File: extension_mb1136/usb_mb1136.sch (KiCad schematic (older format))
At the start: 1 part

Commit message: update schema
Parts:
- added C1: 4.7uF, symbol Device:CP
- added CNUSB_2: USB_A, symbol Connector:USB_A
- added D1: ESDALC6V1-1U2, Diode_SMD:D_0201_0603Metric, symbol Device:D
- added LD1: RED, Diode_SMD:D_0805_2012Metric, symbol Device:LED
- added LD2: GREEN, Diode_SMD:D_0805_2012Metric, symbol Device:LED
- added Q1: S9013, Package_TO_SOT_SMD:SOT-23, symbol Device:Q_NPN_BEC
- added R1: 620, Resistor_SMD:R_0805_2012Metric, symbol Device:R
- added R2, R6: 47K, Resistor_SMD:R_0805_2012Metric, symbol Device:R
- added R3: 430K, Resistor_SMD:R_0805_2012Metric, symbol Device:R
- added R4: 620K, Resistor_SMD:R_0805_2012Metric, symbol Device:R
- added R5: 330, Resistor_SMD:R_0805_2012Metric, symbol Device:R
- added R7: 22K, Resistor_SMD:R_0805_2012Metric, symbol Device:R
- added R7: 10K, Resistor_SMD:R_0805_2012Metric, symbol Device:R
- added U1: STMPS2151MTR, Package_SO:SO-8_3.9x4.9mm_P1.27mm, symbol st:STMPS2151MTR
- renumbered CNUSB to CNUSB_1
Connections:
- net USB_VBUS: now reaches CNUSB_1.1 (VBUS)
- net USB_VBUS: now also C1.1, CNUSB_2.1 (VBUS), R3.1, R6.1, U1.6 (OUT), U1.7 (OUT), U1.8 (OUT)
- net USB_DM: now reaches CNUSB_1.2 (D-)
- net USB_DM: now also CNUSB_2.2 (D-)
- net USB_DP: now reaches CNUSB_1.3 (D+)
- net USB_DP: now also CNUSB_2.3 (D+)
- net USB_ID: now reaches CNUSB_1.4 (ID)
- net USB_ID: now also D1.1 (K)
- net GND: now reaches CNUSB_1.5 (GND)
- net GND: now also CNUSB_1.6 (Shield), C1.2, CNUSB_2.4 (GND), CNUSB_2.5 (Shield), D1.2 (A), Q1.2 (E), R4.2, R7.2, R7.2, U1.1 (GND)
- new net: LD1.2 (A), R1.2
- new net: Q1.1 (B), R6.2, R7.1
- new net: LD2.1 (K), Q1.3 (C)
- new net: LD2.2 (A), R5.2
- new net +3V3: R1.1, R2.1, R5.1
- new net +5V: U1.2 (IN), U1.3 (IN)
- new net USB_OWER_CURRENT: LD1.1 (K), R2.2, U1.5 (~FAULT)
- new net USB_POWER_SWITCH_ON: R7.1, U1.4 (EN)
- new net VBUS_DET: R3.2, R4.1

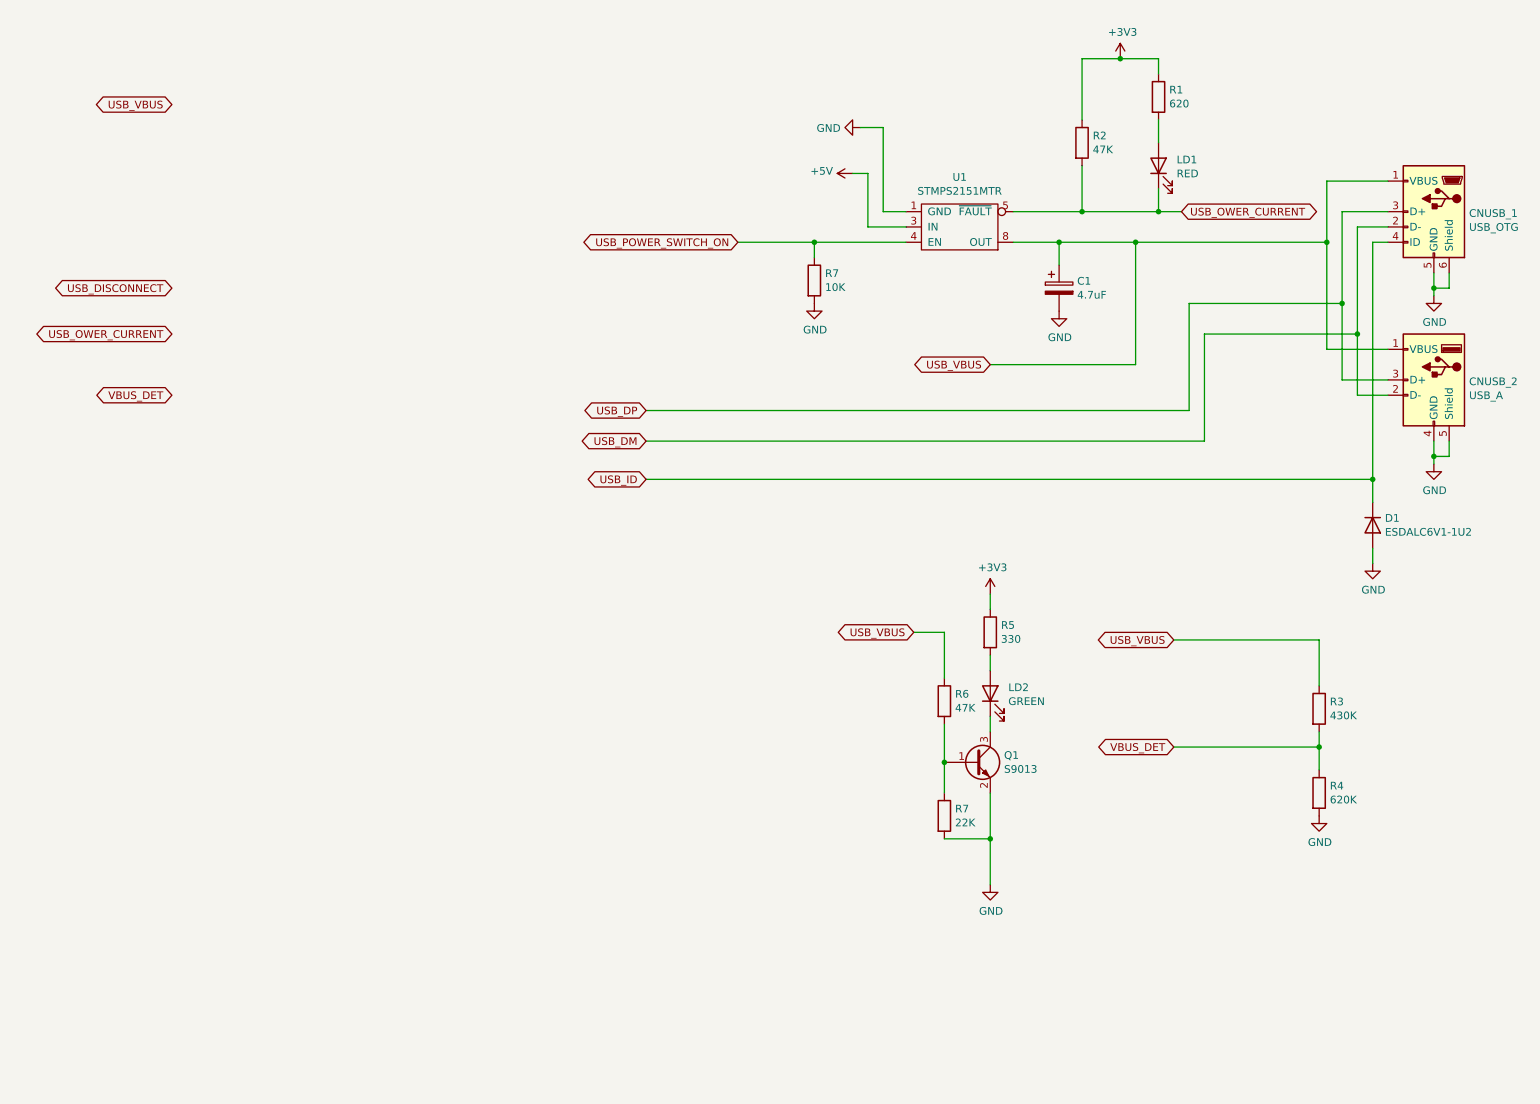
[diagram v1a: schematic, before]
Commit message: USB_connector
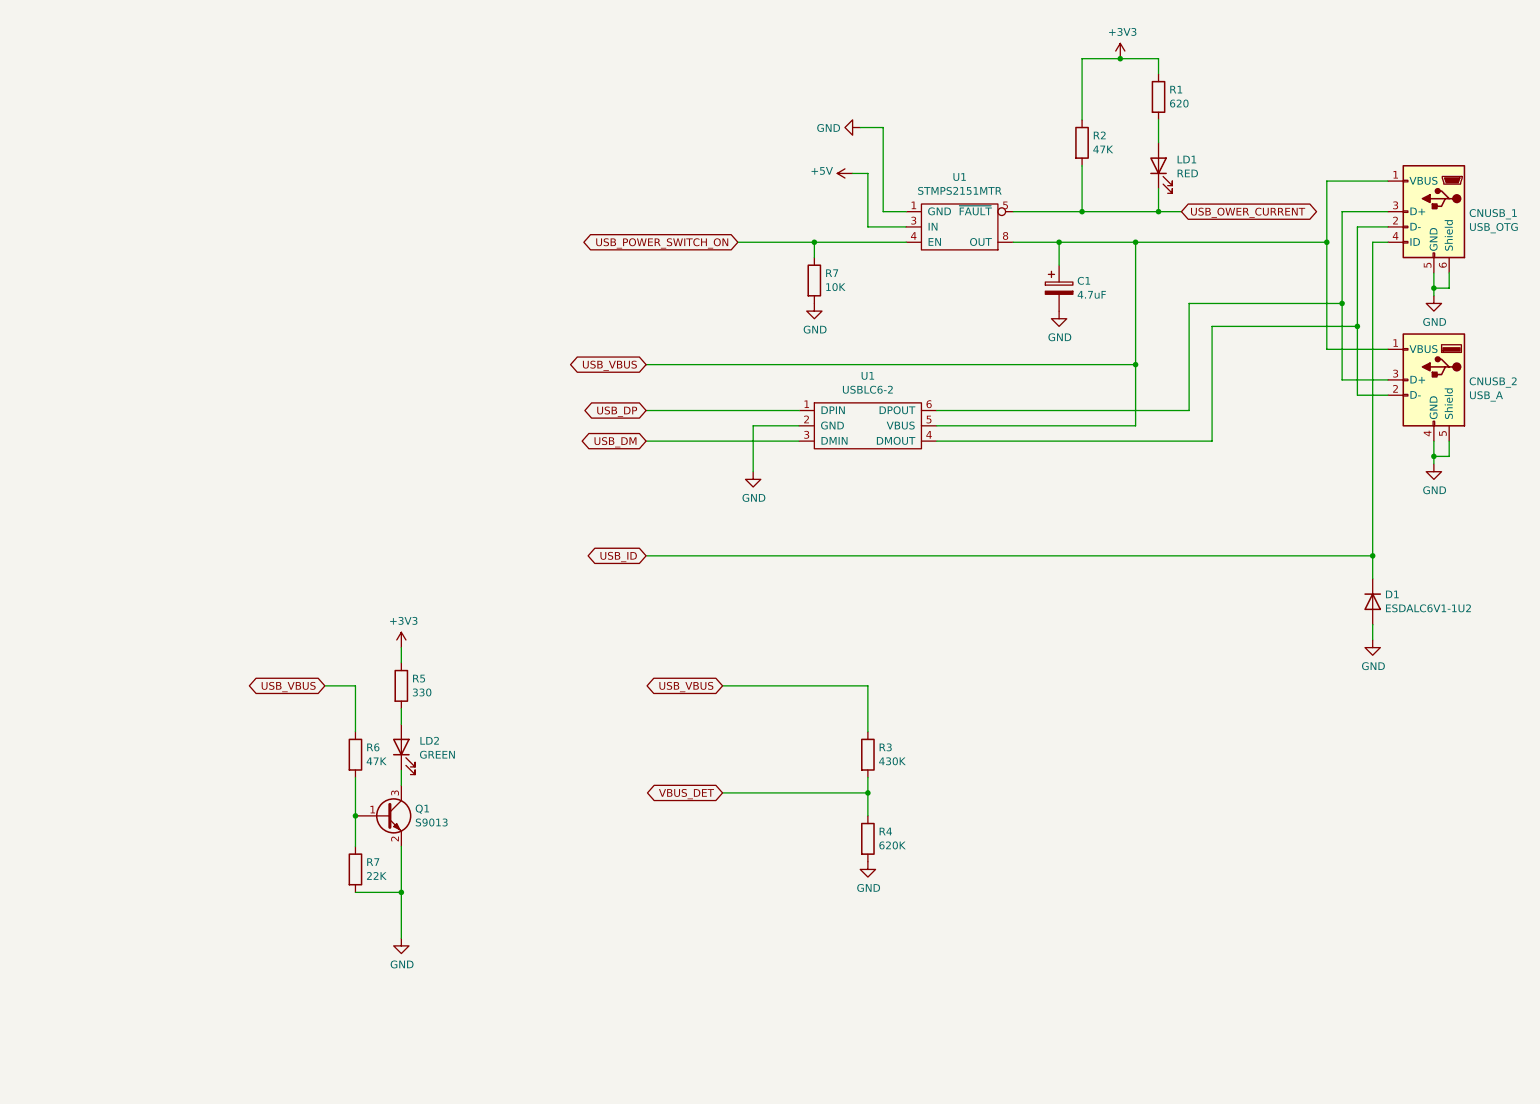
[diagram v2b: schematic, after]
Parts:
- added U1: USBLC6-2, Package_TO_SOT_SMD:SOT-23-6_Handsoldering, symbol st:USBLC6-2
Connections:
- net GND: now also U1.2 (GND)
- net USB_DM: now also U1.3 (DMIN); no longer CNUSB_1.2 (D-), CNUSB_2.2 (D-)
- net USB_DP: now also U1.1 (DPIN); no longer CNUSB_1.3 (D+), CNUSB_2.3 (D+)
- net USB_VBUS: now also U1.5 (VBUS)
- new net: CNUSB_1.2 (D-), CNUSB_2.2 (D-), U1.4 (DMOUT)
- new net: CNUSB_1.3 (D+), CNUSB_2.3 (D+), U1.6 (DPOUT)
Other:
- moved on the sheet: D1, LD2, Q1, R3, R4, R5, R6, R7

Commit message: update
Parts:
- removed U1: USBLC6-2, Package_TO_SOT_SMD:SOT-23-6_Handsoldering, symbol st:USBLC6-2
- added U2: USBLC6-2, Package_TO_SOT_SMD:SOT-23-6_Handsoldering, symbol st:USBLC6-2
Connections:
- net GND: now also U2.2 (GND)
- net USB_DM: now also U2.3 (DMIN)
- net USB_DP: now also U2.1 (DPIN)
- net USB_VBUS: now also U2.5 (VBUS)
- net at CNUSB_1.2 (D-), CNUSB_2.2 (D-): now also U2.4 (DMOUT)
- net at CNUSB_1.3 (D+), CNUSB_2.3 (D+): now also U2.6 (DPOUT)
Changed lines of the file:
@@
 	6550 3400 8350 3400
-$Comp
-L st:USBLC6-2 U1
-U 1 1 5FBFC3C2
-P 6100 3300
-F 0 "U1" H 6100 3625 50  0000 C CNN
-F 1 "USBLC6-2" H 6100 3534 50  0000 C CNN
-F 2 "Package_TO_SOT_SMD:SOT-23-6_Handsoldering" H 6100 3050 50  0001 C CNN
-F 3 "" H 6100 3500 50  0001 C CNN
-	1    6100 3300
-	1    0    0    -1
-$EndComp
 $Comp
 L power:GND #PWR?
@@
 Wire Wire Line
 	4650 2900 7850 2900
+$Comp
+L st:USBLC6-2 U2
+U 1 1 5FBFF8BC
+P 6100 3300
+F 0 "U2" H 6100 3625 50  0000 C CNN
+F 1 "USBLC6-2" H 6100 3534 50  0000 C CNN
+F 2 "Package_TO_SOT_SMD:SOT-23-6_Handsoldering" H 6100 3050 50  0001 C CNN
+F 3 "https://www.st.com/resource/en/datasheet/usblc6-2.pdf" H 6100 3500 50  0001 C CNN
+	1    6100 3300
+	1    0    0    -1
+$EndComp
 $EndSCHEMATC

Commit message: impruve schema
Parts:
- removed U1: STMPS2151MTR, Package_SO:SO-8_3.9x4.9mm_P1.27mm, symbol st:STMPS2151MTR
- added J1, J2: Conn_01x03, Connector_PinHeader_2.54mm:PinHeader_1x03_P2.54mm_Vertical, symbol Connector_Generic:Conn_01x03
- added R9: 1K5, Resistor_SMD:R_0805_2012Metric, symbol Device:R
- renumbered R7 to R3, R5 to R4, R3 to R5, R4 to R7, R7 to R8
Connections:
- net USB_OWER_CURRENT: now also J2.1 (Pin_1)
- net USB_POWER_SWITCH_ON: now also J1.1 (Pin_1)
- net VBUS_DET: now also J2.3 (Pin_3)
- net USB_DM renamed PA11
- net USB_DP renamed PB12
- net PB12: now also R9.1
- net USB_ID renamed PB10
- net USB_VBUS renamed PA9
- new net PC8: J1.2 (Pin_2)
- new net PC9: J2.2 (Pin_2)
- new net USB_DISCONNECT: J1.3 (Pin_3), R9.2
- no-connect marks 0 -> 31
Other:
- moved on the sheet: LD2, Q1, R4, R5, R6, R7, R8

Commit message: add footprint
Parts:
- C1: footprint (none) -> Capacitor_SMD:C_1206_3216Metric
- CNUSB_1: footprint (none) -> Connector_USB:USB_Micro-B_Molex-105017-0001
- CNUSB_2: footprint (none) -> Connector_USB:USB_A_Molex_67643_Horizontal
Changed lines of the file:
@@
 F 0 "CNUSB_1" H 9570 1889 50  0000 R CNN
 F 1 "USB_OTG" H 9570 1798 50  0000 R CNN
-F 2 "" H 9950 1850 50  0001 C CNN
+F 2 "Connector_USB:USB_Micro-B_Molex-105017-0001" H 9950 1850 50  0001 C CNN
 F 3 " ~" H 9950 1850 50  0001 C CNN
 	1    9800 1900
@@
 F 0 "CNUSB_2" H 9570 2989 50  0000 R CNN
 F 1 "USB_A" H 9570 2898 50  0000 R CNN
-F 2 "" H 9950 2950 50  0001 C CNN
+F 2 "Connector_USB:USB_A_Molex_67643_Horizontal" H 9950 2950 50  0001 C CNN
 F 3 " ~" H 9950 2950 50  0001 C CNN
 	1    9800 3000
@@
 F 0 "C1" H 7468 2446 50  0000 L CNN
 F 1 "4.7uF" H 7468 2355 50  0000 L CNN
-F 2 "" H 7388 2250 50  0001 C CNN
+F 2 "Capacitor_SMD:C_1206_3216Metric" H 7388 2250 50  0001 C CNN
 F 3 "~" H 7350 2400 50  0001 C CNN
 	1    7350 2400

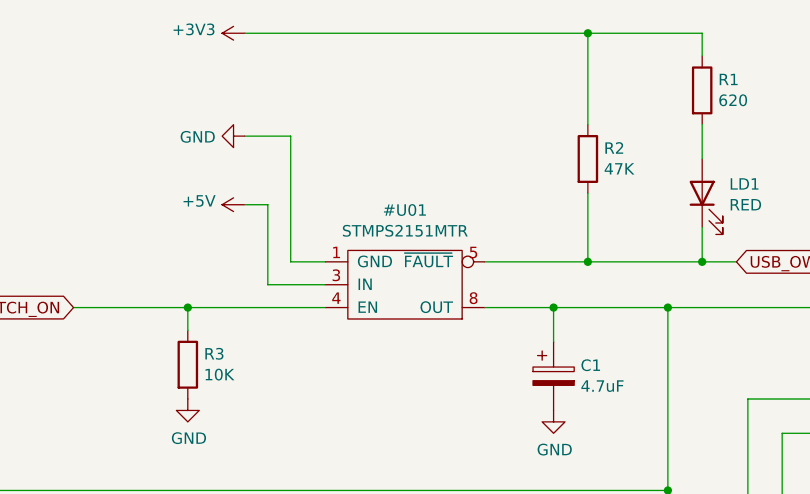
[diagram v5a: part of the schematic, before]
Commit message: add power flags
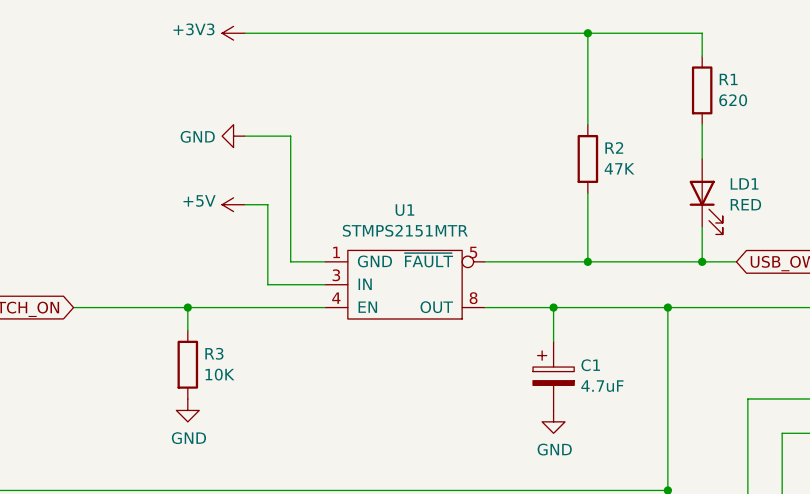
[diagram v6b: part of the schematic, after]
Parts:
- added U1: STMPS2151MTR, Package_SO:SO-8_3.9x4.9mm_P1.27mm, symbol st:STMPS2151MTR
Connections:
- net +5V: now also U1.2 (IN), U1.3 (IN)
- net GND: now also U1.1 (GND)
- net PA9: now also U1.6 (OUT), U1.7 (OUT), U1.8 (OUT)
- net USB_OWER_CURRENT: now also U1.5 (~FAULT)
- net USB_POWER_SWITCH_ON: now also U1.4 (EN)
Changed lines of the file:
@@
 Connection ~ 5850 6350
 $Comp
-L st:STMPS2151MTR #U01
+L st:STMPS2151MTR U1
 U 1 1 5FC77ABB
 P 6700 2000
-F 0 "#U01" H 6700 2325 50  0000 C CNN
+F 0 "U1" H 6700 2325 50  0000 C CNN
 F 1 "STMPS2151MTR" H 6700 2234 50  0000 C CNN
 F 2 "Package_SO:SO-8_3.9x4.9mm_P1.27mm" H 6800 1700 50  0001 C CNN

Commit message: update
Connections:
- net PA9 renamed VBUS
